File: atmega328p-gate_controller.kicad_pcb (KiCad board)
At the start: 2 copper layers, 56.4 x 49.1 mm, 21 parts, among them J1 CONN, J10 PWR, J11 Conn_02x04_Counter_Clockwise, J12 UART, J17 JMP, J18 ISP/SPI, J2 JMP, J4 Conn_02x04_Counter_Clockwise, J8 CONN, J9 CONN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

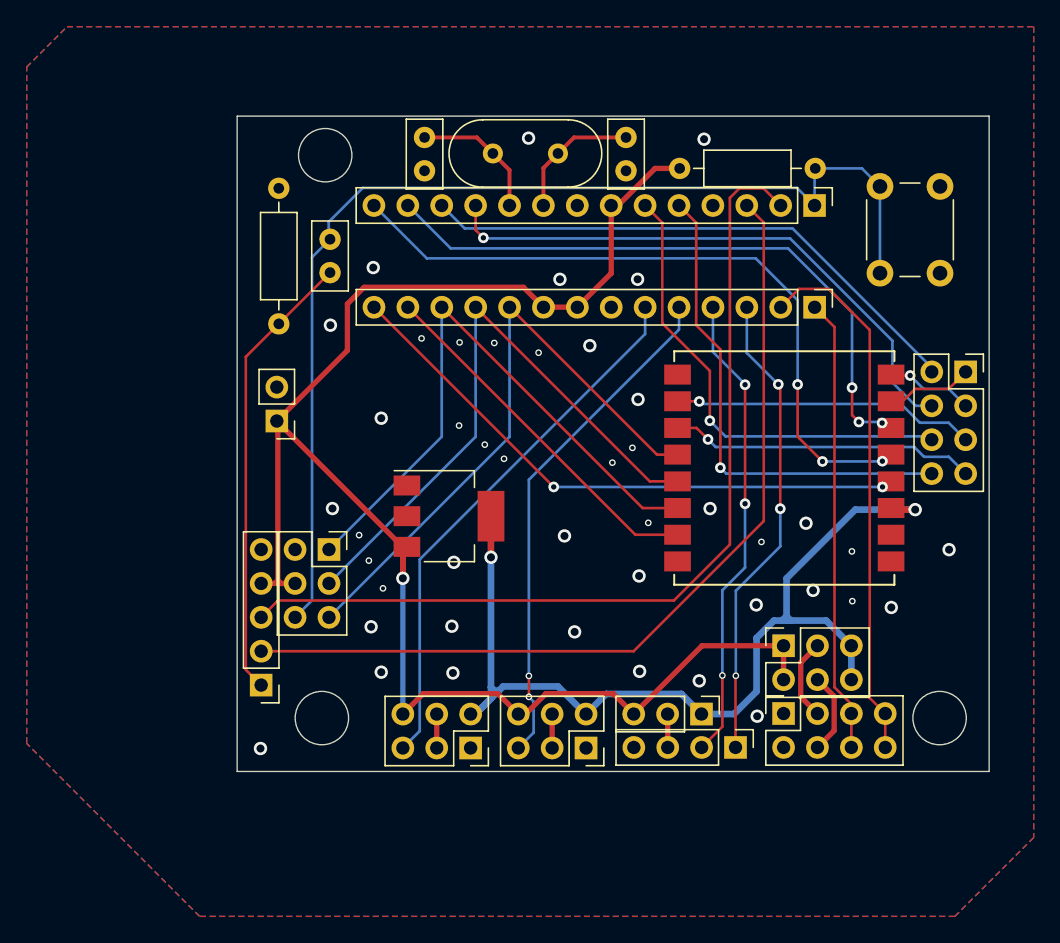
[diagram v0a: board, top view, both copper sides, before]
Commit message: silkscreen done
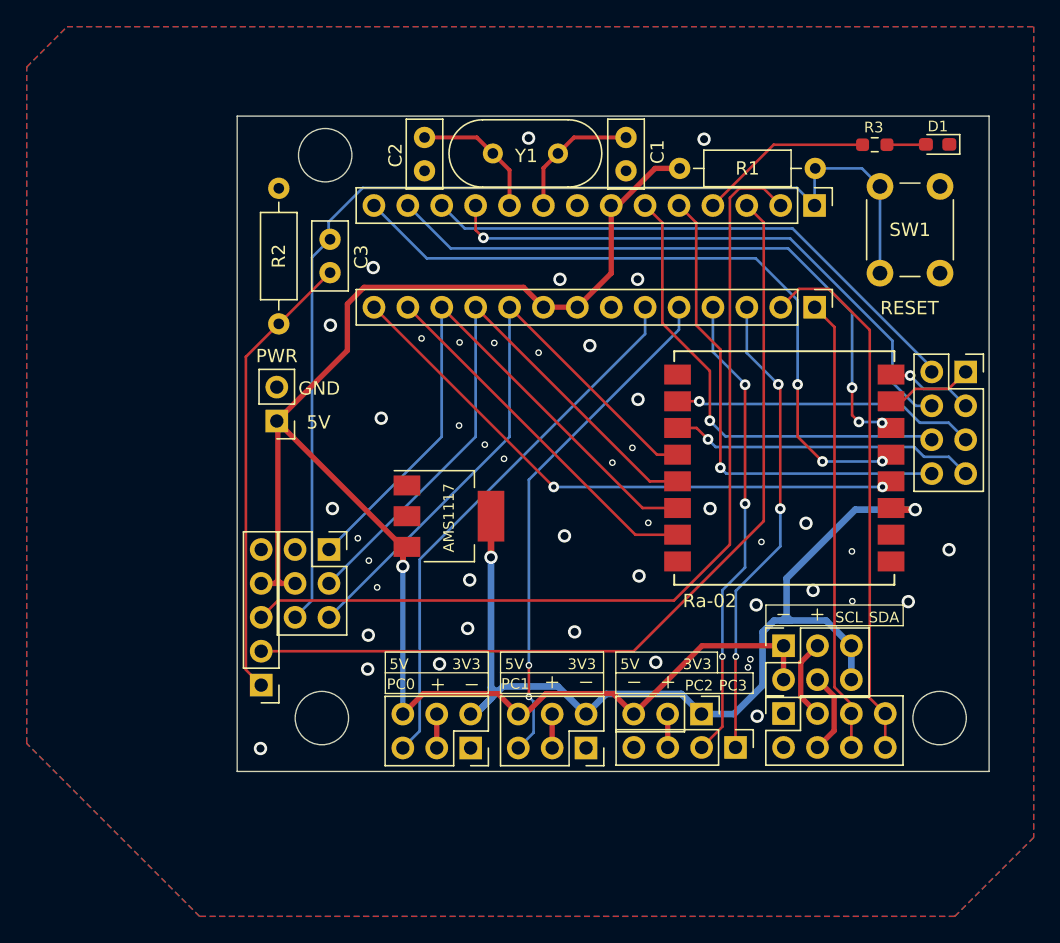
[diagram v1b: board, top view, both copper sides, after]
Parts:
- added D1: LED_Small, LED_SMD:LED_0603_1608Metric_Pad1.05x0.95mm_HandSolder, F.Cu at (149.8, 62.5)
- added R3: 330, Resistor_SMD:R_0603_1608Metric_Pad0.98x0.95mm_HandSolder, F.Cu at (145.1, 62.5)
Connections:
- net /DIO0 renamed /PB0
- net /DIO1 renamed /PD7
- net /PB5 renamed /SCK
- net /PC4 renamed /SDA
- net /PC5 renamed /SCL
- net /PD0 renamed /RX
- net /PD1 renamed /TX
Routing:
- net /PD2: track 0.00 -> 13.1 mm
- net Net-(D1-A): track 0.00 -> 2.93 mm
- net +5V: track 123.6 -> 122.7 mm
- net GND: vias 44 -> 45
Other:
- board text added: "3V3"
- board text added: "5V"
- board text added: "AMS1117"
- board text added: "DTR"
- board text added: "GND"
- board text added: "IO2"
- board text added: "IO3"
- board text added: "IO4"
- board text added: "IO5"
- board text added: "ISP"
- board text added: "MISO"
- board text added: "MOSI"
- board text added: "PC0"
- board text added: "PC1"
- board text added: "PC2"
- board text added: "PC3"
- board text added: "PD3"
- board text added: "PD4"
- board text added: "PD5"
- board text added: "PD6"
- board text added: "RESET"
- board text added: "RST"
- board text added: "RX"
- board text added: "SCK"
- board text added: "SCL"
- board text added: "SDA"
- board text added: "TX"
- board text added: "UART"

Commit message: silkscreen done
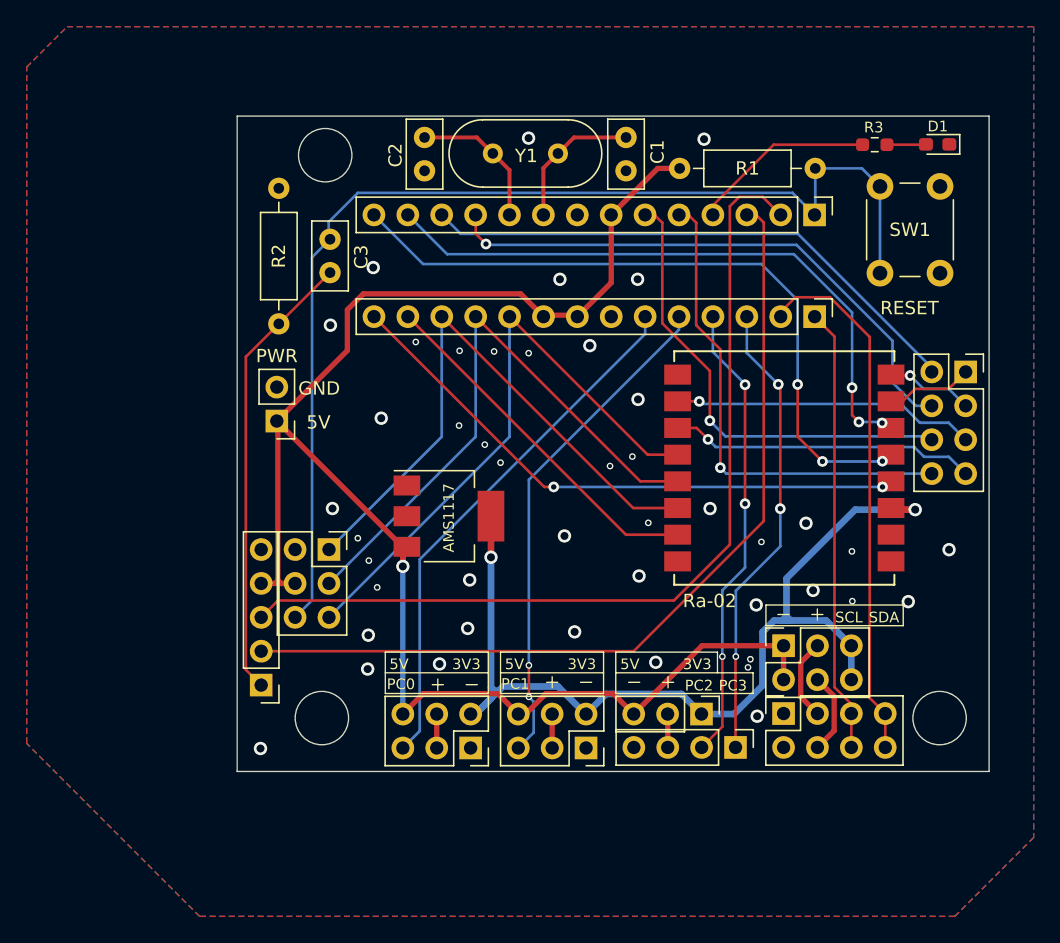
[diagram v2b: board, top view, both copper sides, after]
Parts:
- moved REF** 0.70 mm to (140.6, 75.4)
- moved REF** 0.70 mm to (140.6, 67.8)
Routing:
- net /XTAL1: track 9.95 -> 10.7 mm
- net /PD2: track 13.1 -> 13.8 mm
- net /XTAL2: track 10.0 -> 10.7 mm
- net /RESET: track 83.4 -> 84.1 mm
- net /RX: track 68.0 -> 67.4 mm

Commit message: done
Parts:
- added G***: LOGO, LOGO, B.Cu at (126.1, 98.3)
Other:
- board text added: "ATmega168/328 Gate Controller"
- board text added: "Designed by:"

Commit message: kikit tabs
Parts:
- added REF**: Tab, kikit:Tab, F.Cu at (116.9, 111.6)
- added REF**: Tab, kikit:Tab, F.Cu at (116.9, 54.7)
- added REF**: Tab, kikit:Tab, F.Cu at (144.9, 54.7)
- added REF**: Tab, kikit:Tab, F.Cu at (155.8, 66.1)
- added REF**: Tab, kikit:Tab, F.Cu at (106.0, 100.3)
- added REF**: Tab, kikit:Tab, F.Cu at (144.9, 111.6)
- added REF**: Tab, kikit:Tab, F.Cu at (106.1, 66.1)
- added REF**: Tab, kikit:Tab, F.Cu at (155.8, 100.3)
- moved R2 50.2 mm to (150.0, 58.1), turned to 180 degrees
- moved J12 48.2 mm to (112.8, 56.8), turned to 90 degrees
- moved D1 45.1 mm to (153.3, 107.5), turned to 90 degrees
- moved R3 41.1 mm to (153.3, 102.8), turned to 90 degrees
- moved J10 41.0 mm to (132.6, 58.0), turned to 90 degrees
- moved C3 40.7 mm to (143.7, 62.0), turned to 0 degrees
- moved C2 40.2 mm to (151.4, 69.0), turned to 0 degrees
- moved J18 36.2 mm to (123.0, 61.9), turned to -90 degrees
- moved J8 35.9 mm to (108.1, 72.5), turned to 180 degrees
- moved R1 35.7 mm to (151.5, 98.3), turned to 90 degrees
- moved C1 35.2 mm to (153.9, 84.2), turned to 180 degrees
- moved Y1 35.1 mm to (152.7, 79.0), turned to 90 degrees
- moved J4 33.9 mm to (136.3, 109.6), turned to -90 degrees
- moved REF** 31.4 mm to (148.0, 98.3), turned to 180 degrees
- moved SW1 31.1 mm to (143.7, 103.2), turned to 0 degrees
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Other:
- board size 56.4 x 49.1 mm -> 49.1 x 56.4 mm
